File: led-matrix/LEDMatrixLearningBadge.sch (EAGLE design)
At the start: 95 parts, among them IC1 5M40ZE64, IC2 MEGA48/88/168-MU, Q1 HM4522P-423-G, SW1 4_DIRECTIONAL_JOYSTICK_PLUS_C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, T1 ZXM61P03, T10 ZXM61P03, T11 ZXM61P03, T12 ZXM61P03, T13 ZXM61P03, T14 ZXM61P03, T15 ZXM61P03, T16 ZXM61P03, T17 DMN65D8L, T18 DMN65D8L, T19 DMN65D8L, T2 ZXM61P03, T20 DMN65D8L, T21 DMN65D8L, T22 DMN65D8L, T23 DMN65D8L, T24 DMN65D8L, T25 DMN65D8L, T26 DMN65D8L, T27 DMN65D8L, T28 DMN65D8L, T29 DMN65D8L, T3 ZXM61P03, T30 DMN65D8L, T31 DMN65D8L, T32 DMN65D8L, T4 ZXM61P03, T5 ZXM61P03, T6 ZXM61P03, T7 ZXM61P03, T8 ZXM61P03, T9 ZXM61P03, U1 FT440-FIXED, U2 MCP6L01, Y1 8MHz

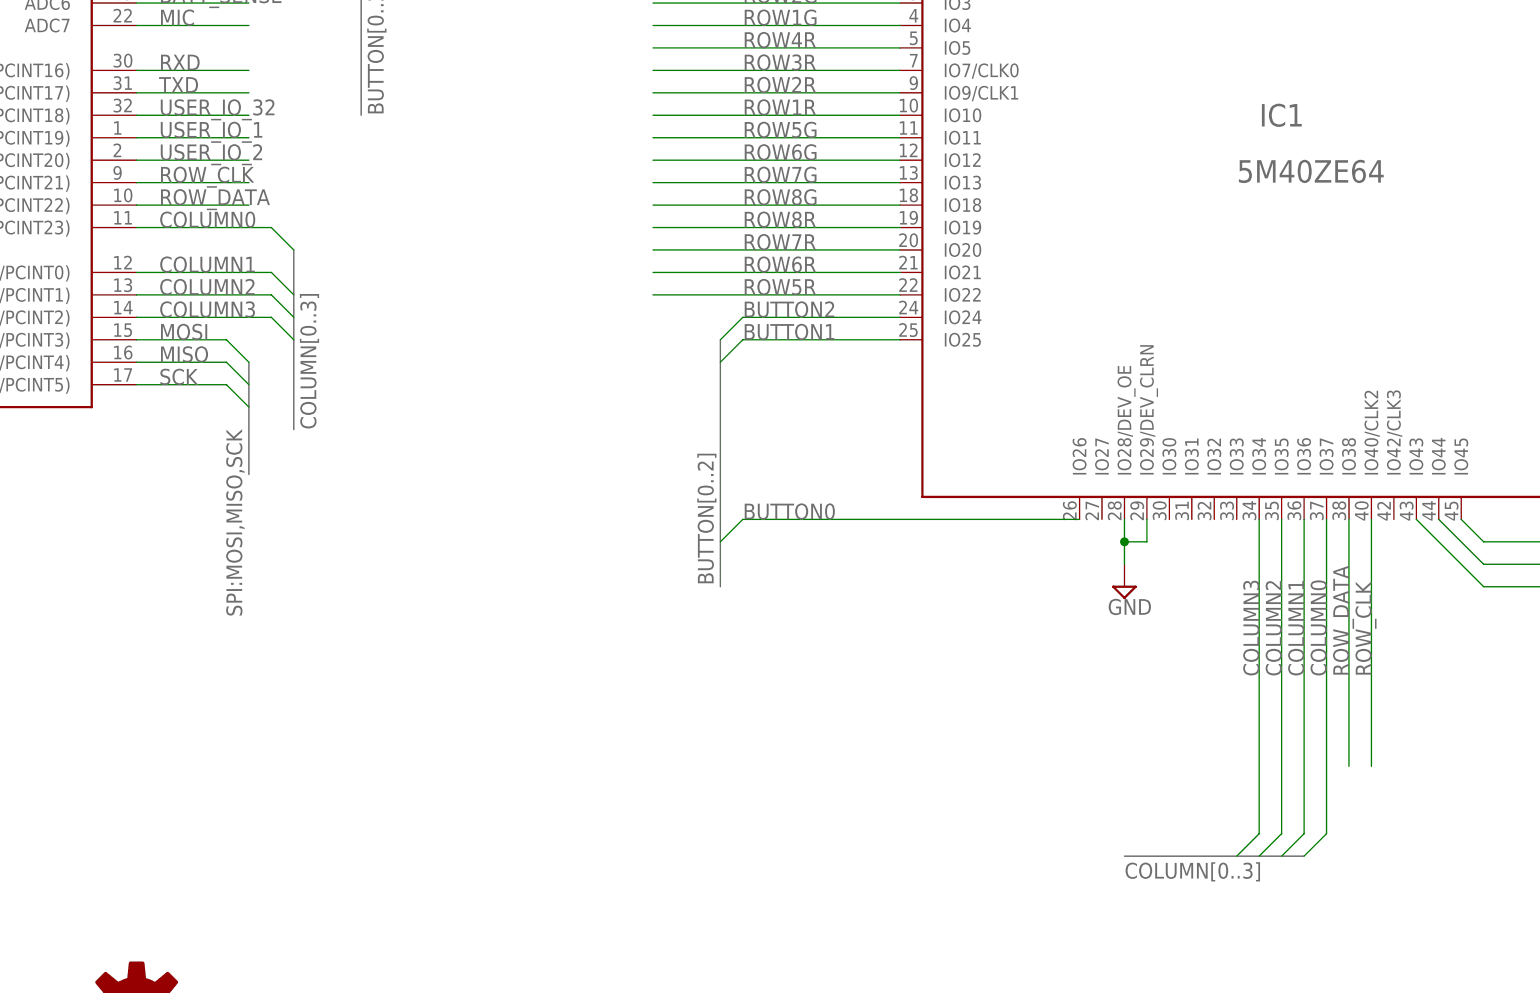
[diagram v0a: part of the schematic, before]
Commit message: Signal rename
Renamed CPLD signals to cpu to reflect reworked hdl code
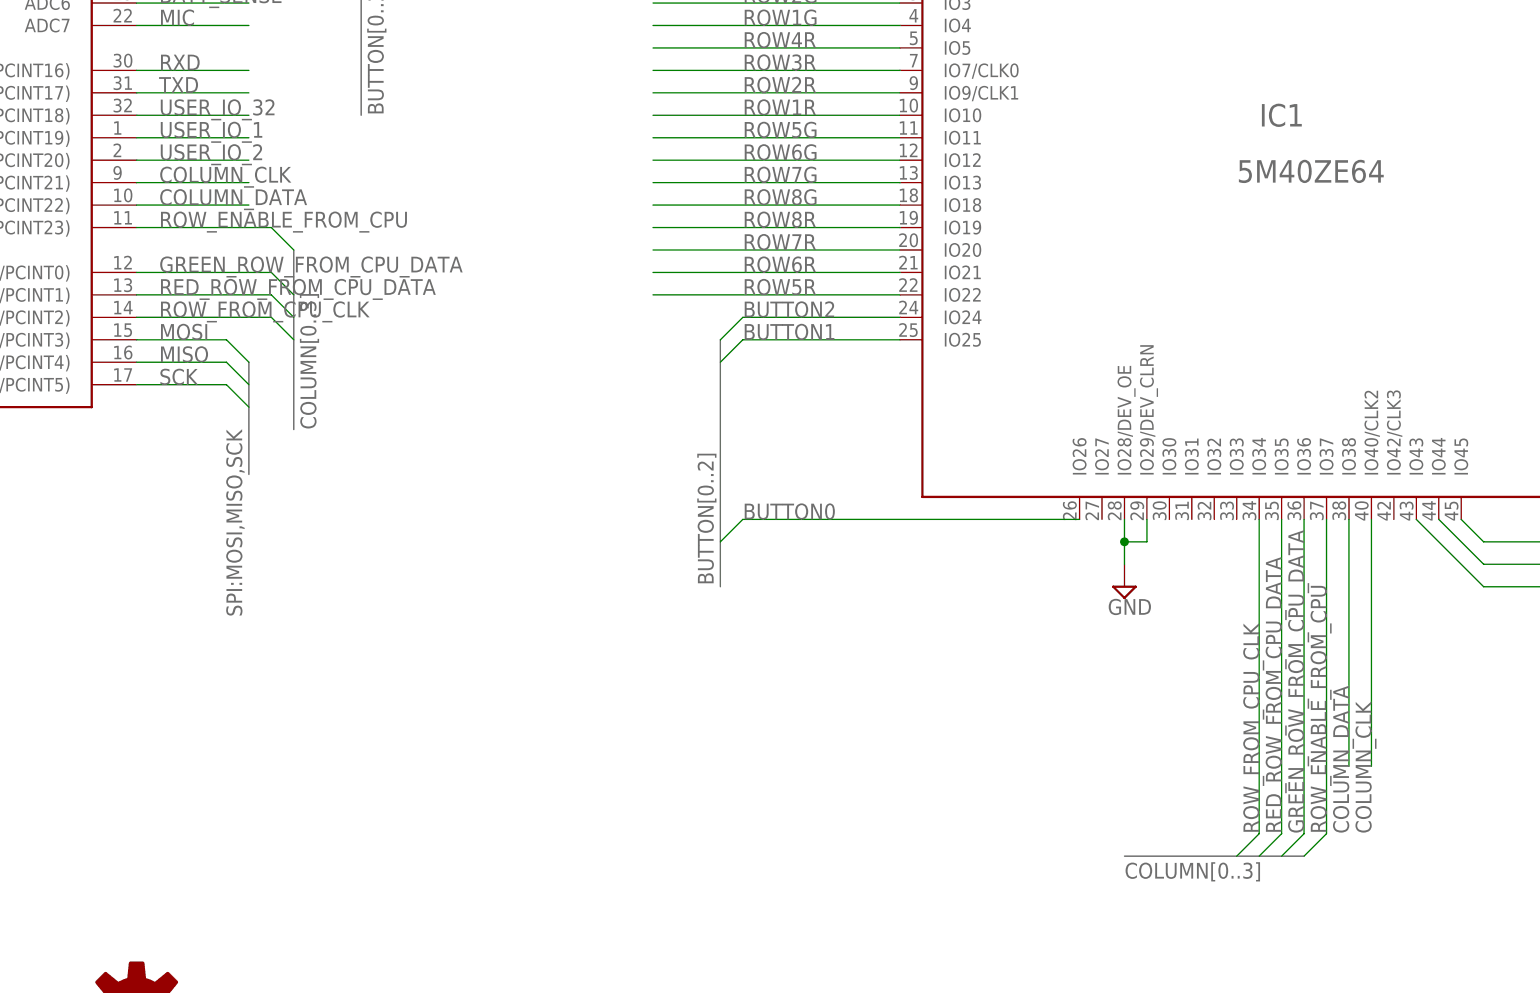
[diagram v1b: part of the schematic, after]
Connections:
- net COLUMN0 renamed ROW_ENABLE_FROM_CPU
- net COLUMN1 renamed GREEN_ROW_FROM_CPU_DATA
- net COLUMN2 renamed RED_ROW_FROM_CPU_DATA
- net COLUMN3 renamed ROW_FROM_CPU_CLK
- net ROW_CLK renamed COLUMN_CLK
- net ROW_DATA renamed COLUMN_DATA
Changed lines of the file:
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@@
 </segment>
 </net>
-<net name="ROW_DATA" class="0">
+<net name="COLUMN_DATA" class="0">
 <segment>
 <wire x1="205.74" y1="119.38" x2="218.44" y2="119.38" width="0.1524" layer="91"/>
@@
 </segment>
 <segment>
-<label x="342.9" y="66.04" size="1.778" layer="95" rot="R90"/>
+<label x="342.9" y="48.26" size="1.778" layer="95" rot="R90"/>
 <wire x1="342.9" y1="55.88" x2="342.9" y2="83.82" width="0.1524" layer="91"/>
 <pinref part="IC1" gate="G$1" pin="IO38"/>
 </segment>
 </net>
-<net name="ROW_CLK" class="0">
+<net name="COLUMN_CLK" class="0">
 <segment>
 <wire x1="205.74" y1="121.92" x2="218.44" y2="121.92" width="0.1524" layer="91"/>
@@
 <segment>
 <wire x1="345.44" y1="83.82" x2="345.44" y2="55.88" width="0.1524" layer="91"/>
-<label x="345.44" y="66.04" size="1.778" layer="95" rot="R90"/>
+<label x="345.44" y="48.26" size="1.778" layer="95" rot="R90"/>
 <pinref part="IC1" gate="G$1" pin="IO40/CLK2"/>
 </segment>
 </net>
-<net name="COLUMN0" class="0">
+<net name="ROW_ENABLE_FROM_CPU" class="0">
 <segment>
 <pinref part="IC2" gate="1" pin="PD7(AIN1/PCINT23)"/>
@@
 <wire x1="337.82" y1="45.72" x2="340.36" y2="48.26" width="0.1524" layer="91"/>
 <wire x1="340.36" y1="48.26" x2="340.36" y2="83.82" width="0.1524" layer="91"/>
-<label x="340.36" y="66.04" size="1.778" layer="95" rot="R90"/>
+<label x="340.36" y="48.26" size="1.778" layer="95" rot="R90"/>
 </segment>
 </net>
-<net name="COLUMN1" class="0">
+<net name="GREEN_ROW_FROM_CPU_DATA" class="0">
 <segment>
 <pinref part="IC2" gate="1" pin="PB0(ICP1/CLKO/PCINT0)"/>
@@
 <wire x1="335.28" y1="45.72" x2="337.82" y2="48.26" width="0.1524" layer="91"/>
 <wire x1="337.82" y1="48.26" x2="337.82" y2="83.82" width="0.1524" layer="91"/>
-<label x="337.82" y="66.04" size="1.778" layer="95" rot="R90"/>
+<label x="337.82" y="48.26" size="1.778" layer="95" rot="R90"/>
 </segment>
 </net>
-<net name="COLUMN2" class="0">
+<net name="RED_ROW_FROM_CPU_DATA" class="0">
 <segment>
 <pinref part="IC2" gate="1" pin="PB1(OC1A/PCINT1)"/>
@@
 <wire x1="332.74" y1="45.72" x2="335.28" y2="48.26" width="0.1524" layer="91"/>
 <wire x1="335.28" y1="48.26" x2="335.28" y2="83.82" width="0.1524" layer="91"/>
-<label x="335.28" y="66.04" size="1.778" layer="95" rot="R90"/>
+<label x="335.28" y="48.26" size="1.778" layer="95" rot="R90"/>
 </segment>
 </net>
-<net name="COLUMN3" class="0">
+<net name="ROW_FROM_CPU_CLK" class="0">
 <segment>
 <pinref part="IC2" gate="1" pin="PB2(SS/OC1B/PCINT2)"/>
@@
 <wire x1="330.2" y1="45.72" x2="332.74" y2="48.26" width="0.1524" layer="91"/>
 <wire x1="332.74" y1="48.26" x2="332.74" y2="83.82" width="0.1524" layer="91"/>
-<label x="332.74" y="66.04" size="1.778" layer="95" rot="R90"/>
+<label x="332.74" y="48.26" size="1.778" layer="95" rot="R90"/>
 </segment>
 </net>
